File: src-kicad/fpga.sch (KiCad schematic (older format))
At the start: 28 parts, among them U1 iCE40HX1K-TQ144, U2 N25Q032A

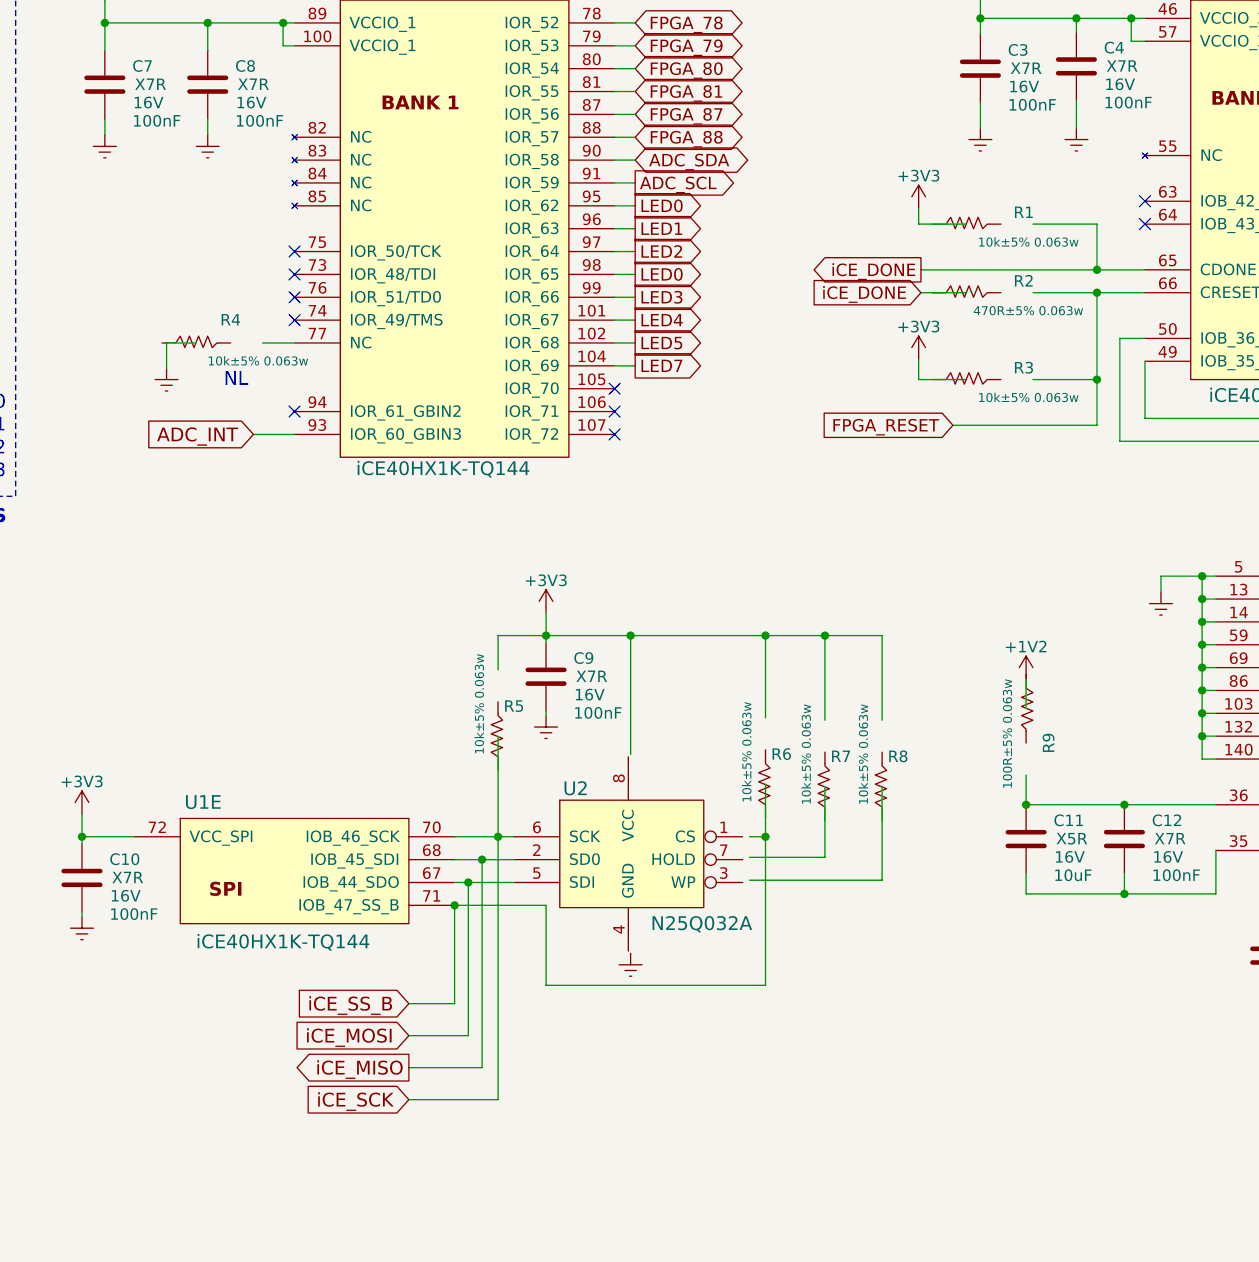
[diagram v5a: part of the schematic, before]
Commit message: Kicad migration: user peripherals added to schematic
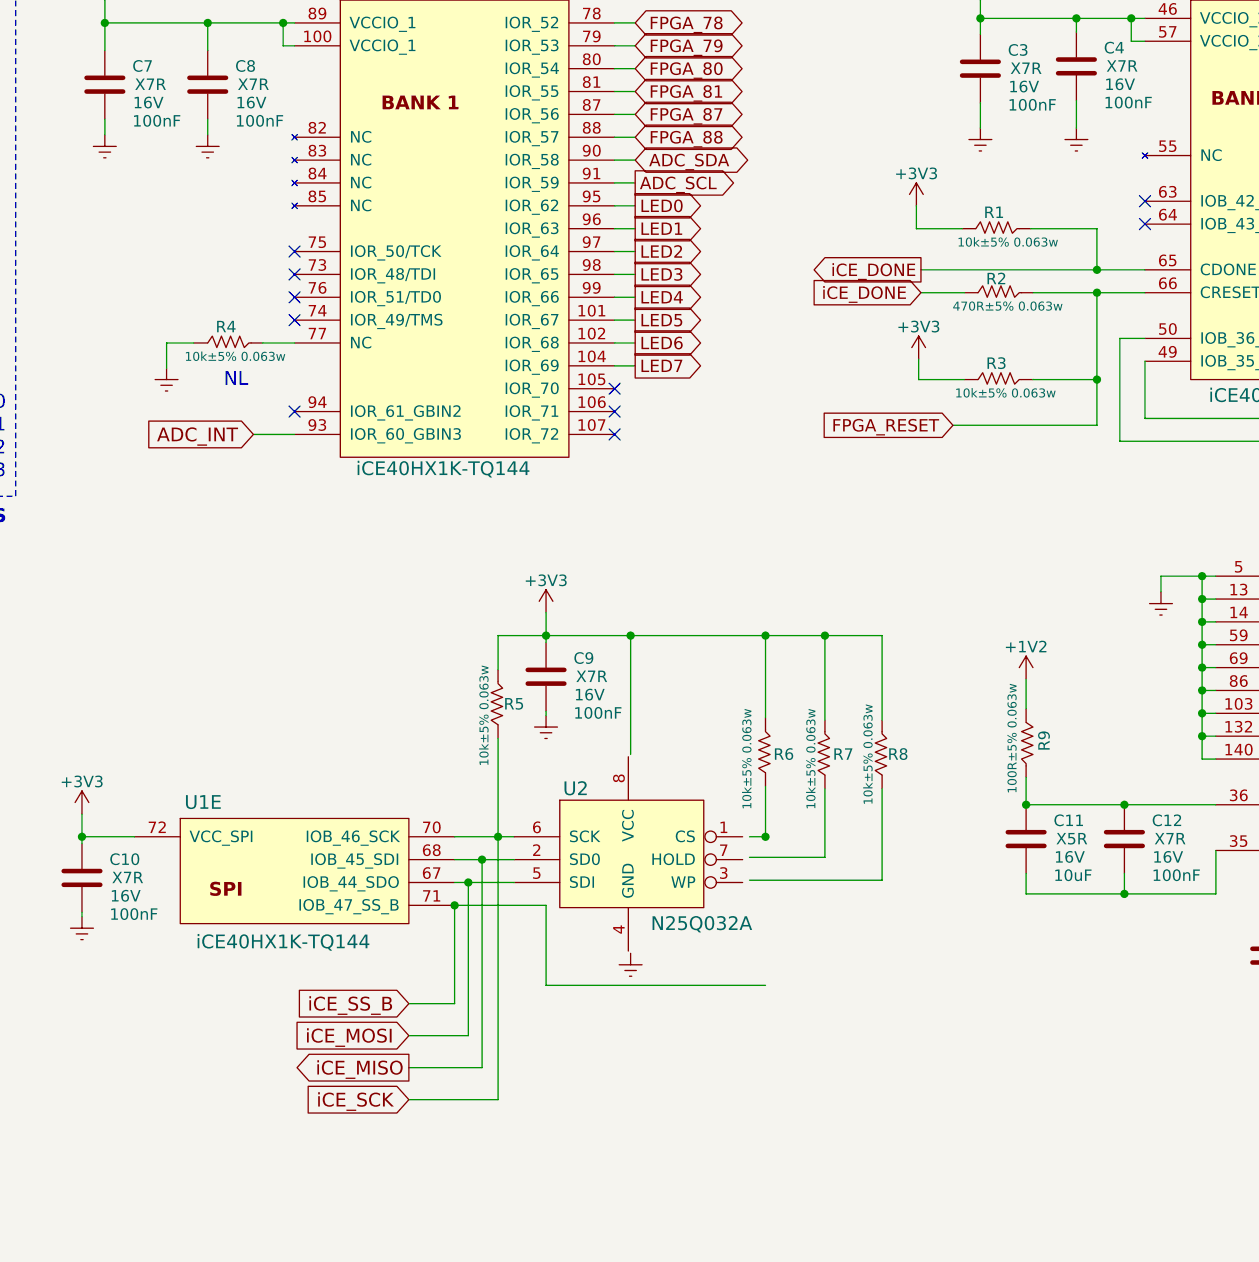
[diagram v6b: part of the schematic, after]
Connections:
- net labels added: LED6
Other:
- moved on the sheet: R1, R2, R3, R4, R5, R6, R7, R8, R9
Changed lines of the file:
@@
 LIBS:[4]_Power_Supply-cache
 LIBS:[4]_Power_Supply-rescue
+LIBS:[3]_Connectors_&_IO-cache
 LIBS:icezum-cache
 EELAYER 25 0
@@
 $Descr A4 11693 8268
 encoding utf-8
-Sheet 2 4
+Sheet 2 5
 Title "Icezum Alhambra"
 Date "2016-05-23"
@@
 L R R4
 U 1 1 574319A2
-P 4650 2300
-F 0 "R4" V 4550 2300 50  0000 C CNN
-F 1 "10k±5% 0.063w" V 4730 2420 39  0000 C CNN
-F 2 "" V 4580 2300 50  0000 C CNN
-F 3 "" H 4650 2300 50  0000 C CNN
-	1    4650 2300
+P 4790 2300
+F 0 "R4" V 4720 2140 50  0000 C CNN
+F 1 "10k±5% 0.063w" V 4850 2180 39  0000 C CNN
+F 2 "" V 4720 2300 50  0000 C CNN
+F 3 "" H 4790 2300 50  0000 C CNN
+	1    4790 2300
 	0    1    1    0
 $EndComp
@@
 LED2
 Text GLabel 6420 2000 2    54   Output ~ 0
-LED0
+LED3
 Text GLabel 6420 2100 2    54   Output ~ 0
-LED3
+LED4
 Text GLabel 6420 2200 2    54   Output ~ 0
-LED4
+LED5
 Text GLabel 6420 2300 2    54   Output ~ 0
-LED5
+LED6
 Text GLabel 6420 2400 2    54   Output ~ 0
 LED7
@@
 L R R2
 U 1 1 57438123
-P 8020 2080
-F 0 "R2" V 7970 2180 50  0000 C CNN
-F 1 "470R±5% 0.063w" V 8100 2200 39  0000 C CNN
-F 2 "" V 7950 2080 50  0000 C CNN
-F 3 "" H 8020 2080 50  0000 C CNN
-	1    8020 2080
+P 8160 2080
+F 0 "R2" V 8100 1920 50  0000 C CNN
+F 1 "470R±5% 0.063w" V 8220 1970 39  0000 C CNN
+F 2 "" V 8090 2080 50  0000 C CNN
+F 3 "" H 8160 2080 50  0000 C CNN
+	1    8160 2080
 	0    1    1    0
 $EndComp
@@
 L +3V3 #PWR011
 U 1 1 5743856A
-P 7660 1710
-F 0 "#PWR011" H 7660 1560 50  0001 C CNN
-F 1 "+3V3" H 7660 1850 50  0000 C CNN
-F 2 "" H 7660 1710 50  0000 C CNN
-F 3 "" H 7660 1710 50  0000 C CNN
-	1    7660 1710
-	1    0    0    -1
-$EndComp
-$Comp
-L R R1
-U 1 1 57438596
-P 8020 1780
-F 0 "R1" V 7970 1880 50  0000 C CNN
-F 1 "10k±5% 0.063w" V 8100 1900 39  0000 C CNN
-F 2 "" V 7950 1780 50  0000 C CNN
-F 3 "" H 8020 1780 50  0000 C CNN
-	1    8020 1780
-	0    1    1    0
+P 7650 1700
+F 0 "#PWR011" H 7650 1550 50  0001 C CNN
+F 1 "+3V3" H 7650 1840 50  0000 C CNN
+F 2 "" H 7650 1700 50  0000 C CNN
+F 3 "" H 7650 1700 50  0000 C CNN
+	1    7650 1700
+	1    0    0    -1
 $EndComp
 $Comp
@@
 L R R3
 U 1 1 57438C6A
-P 8020 2460
-F 0 "R3" V 7970 2560 50  0000 C CNN
-F 1 "10k±5% 0.063w" V 8100 2580 39  0000 C CNN
-F 2 "" V 7950 2460 50  0000 C CNN
-F 3 "" H 8020 2460 50  0000 C CNN
-	1    8020 2460
+P 8160 2460
+F 0 "R3" V 8090 2300 50  0000 C CNN
+F 1 "10k±5% 0.063w" V 8220 2340 39  0000 C CNN
+F 2 "" V 8090 2460 50  0000 C CNN
+F 3 "" H 8160 2460 50  0000 C CNN
+	1    8160 2460
 	0    1    1    0
 $EndComp
@@
 L R R9
 U 1 1 574481A7
-P 8130 4050
-F 0 "R9" V 8030 4050 50  0000 C CNN
-F 1 "100R±5% 0.063w" V 8210 4010 39  0000 C CNN
-F 2 "" V 8060 4050 50  0000 C CNN
-F 3 "" H 8130 4050 50  0000 C CNN
-	1    8130 4050
+P 8130 4200
+F 0 "R9" V 8050 4040 50  0000 C CNN
+F 1 "100R±5% 0.063w" V 8190 4030 39  0000 C CNN
+F 2 "" V 8060 4200 50  0000 C CNN
+F 3 "" H 8130 4200 50  0000 C CNN
+	1    8130 4200
 	-1   0    0    1
 $EndComp
@@
 L R R6
 U 1 1 574429CE
-P 6990 4080
-F 0 "R6" H 7060 4060 50  0000 C CNN
-F 1 "10k±5% 0.063w" V 6910 4070 39  0000 C CNN
-F 2 "" V 6920 4080 50  0000 C CNN
-F 3 "" H 6990 4080 50  0000 C CNN
-	1    6990 4080
+P 6990 3940
+F 0 "R6" H 7070 3780 50  0000 C CNN
+F 1 "10k±5% 0.063w" V 6910 3760 39  0000 C CNN
+F 2 "" V 6920 3940 50  0000 C CNN
+F 3 "" H 6990 3940 50  0000 C CNN
+	1    6990 3940
 	1    0    0    -1
 $EndComp
@@
 L R R7
 U 1 1 57447BC5
-P 7250 4090
-F 0 "R7" H 7320 4070 50  0000 C CNN
-F 1 "10k±5% 0.063w" V 7170 4080 39  0000 C CNN
-F 2 "" V 7180 4090 50  0000 C CNN
-F 3 "" H 7250 4090 50  0000 C CNN
-	1    7250 4090
+P 7250 3950
+F 0 "R7" H 7330 3800 50  0000 C CNN
+F 1 "10k±5% 0.063w" V 7190 3780 39  0000 C CNN
+F 2 "" V 7180 3950 50  0000 C CNN
+F 3 "" H 7250 3950 50  0000 C CNN
+	1    7250 3950
 	1    0    0    -1
 $EndComp
@@
 L R R8
 U 1 1 57447C61
-P 7500 4090
-F 0 "R8" H 7570 4070 50  0000 C CNN
-F 1 "10k±5% 0.063w" V 7420 4080 39  0000 C CNN
-F 2 "" V 7430 4090 50  0000 C CNN
-F 3 "" H 7500 4090 50  0000 C CNN
-	1    7500 4090
+P 7500 3950
+F 0 "R8" H 7570 3800 50  0000 C CNN
+F 1 "10k±5% 0.063w" V 7440 3800 39  0000 C CNN
+F 2 "" V 7430 3950 50  0000 C CNN
+F 3 "" H 7500 3950 50  0000 C CNN
+	1    7500 3950
 	1    0    0    -1
 $EndComp
@@
 L R R5
 U 1 1 57448214
-P 5820 3870
-F 0 "R5" H 5890 3850 50  0000 C CNN
-F 1 "10k±5% 0.063w" V 5740 3860 39  0000 C CNN
-F 2 "" V 5750 3870 50  0000 C CNN
-F 3 "" H 5820 3870 50  0000 C CNN
-	1    5820 3870
+P 5820 3730
+F 0 "R5" H 5890 3580 50  0000 C CNN
+F 1 "10k±5% 0.063w" V 5760 3530 39  0000 C CNN
+F 2 "" V 5750 3730 50  0000 C CNN
+F 3 "" H 5820 3730 50  0000 C CNN
+	1    5820 3730
 	1    0    0    -1
 $EndComp
@@
 	4790 2300 4930 2300
 Wire Wire Line
-	4500 2300 4370 2300
-Wire Wire Line
 	6420 900  6330 900
 Wire Wire Line
@@
 	7670 1980 8650 1980
 Wire Wire Line
-	7660 1710 7660 1780
-Wire Wire Line
-	7660 1780 7870 1780
-Wire Wire Line
-	7870 2080 7670 2080
-Wire Wire Line
 	8160 2080 8650 2080
-Wire Wire Line
-	8160 1780 8440 1780
 Connection ~ 8440 1980
 Wire Wire Line
 	7660 2370 7660 2460
-Wire Wire Line
-	7660 2460 7870 2460
 Wire Wire Line
 	8440 2660 7810 2660
@@
 	8160 2460 8440 2460
 Connection ~ 8440 2460
-Wire Wire Line
-	8440 1780 8440 1980
 Wire Wire Line
 	8440 2080 8440 2660
@@
 	10860 3420 10860 3220
 Wire Wire Line
-	8130 4190 8130 4320
-Wire Wire Line
 	8130 3770 8130 3900
 Connection ~ 8130 4320
@@
 	5630 4460 5890 4460
 Wire Wire Line
-	5820 4020 5820 5610
-Wire Wire Line
 	6990 3580 6990 3940
 Connection ~ 6400 3580
@@
 	6920 4460 6990 4460
 Wire Wire Line
-	6990 4230 6990 5110
-Wire Wire Line
 	6920 4550 7250 4550
 Wire Wire Line
-	7250 4550 7250 4240
-Wire Wire Line
 	6920 4650 7500 4650
-Wire Wire Line
-	7500 4650 7500 4240
 Wire Wire Line
 	5430 5190 5630 5190
@@
 Text Notes 2940 3100 0    60   ~ 12
 iCEZUM IO PINS
+$Comp
+L R R1
+U 1 1 57438596
+P 8150 1800
+F 0 "R1" V 8080 1640 50  0000 C CNN
+F 1 "10k±5% 0.063w" V 8210 1700 39  0000 C CNN
+F 2 "" V 8080 1800 50  0000 C CNN
+F 3 "" H 8150 1800 50  0000 C CNN
+	1    8150 1800
+	0    1    1    0
+$EndComp
+Wire Wire Line
+	7650 1700 7650 1800
+Wire Wire Line
+	7650 1800 7850 1800
+Wire Wire Line
+	8150 1800 8440 1800
+Wire Wire Line
+	8440 1800 8440 1980
+Wire Wire Line
+	7670 2080 7860 2080
+Wire Wire Line
+	7660 2460 7860 2460
+Wire Wire Line
+	8130 4320 8130 4200
+Wire Wire Line
+	7500 4650 7500 4250
+Wire Wire Line
+	7250 4550 7250 4250
+Wire Wire Line
+	6990 4460 6990 4240
+Wire Wire Line
+	5820 4030 5820 5610
+Wire Wire Line
+	4370 2300 4490 2300
 $EndSCHEMATC
